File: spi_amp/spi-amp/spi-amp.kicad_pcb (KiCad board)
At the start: 4 copper layers, 26.9 x 69.3 mm, 37 parts, among them J1 IN+, J2 IN-, J3 OUT+, J4 OUT-, J5 Conn_01x02, J7 Conn_01x06, U1 LMH6401, U2 LM78M05_TO220, U3 LTV-847S, U4 74LVC1G04, U5 74LVC1G04, U6 74LVC1G04

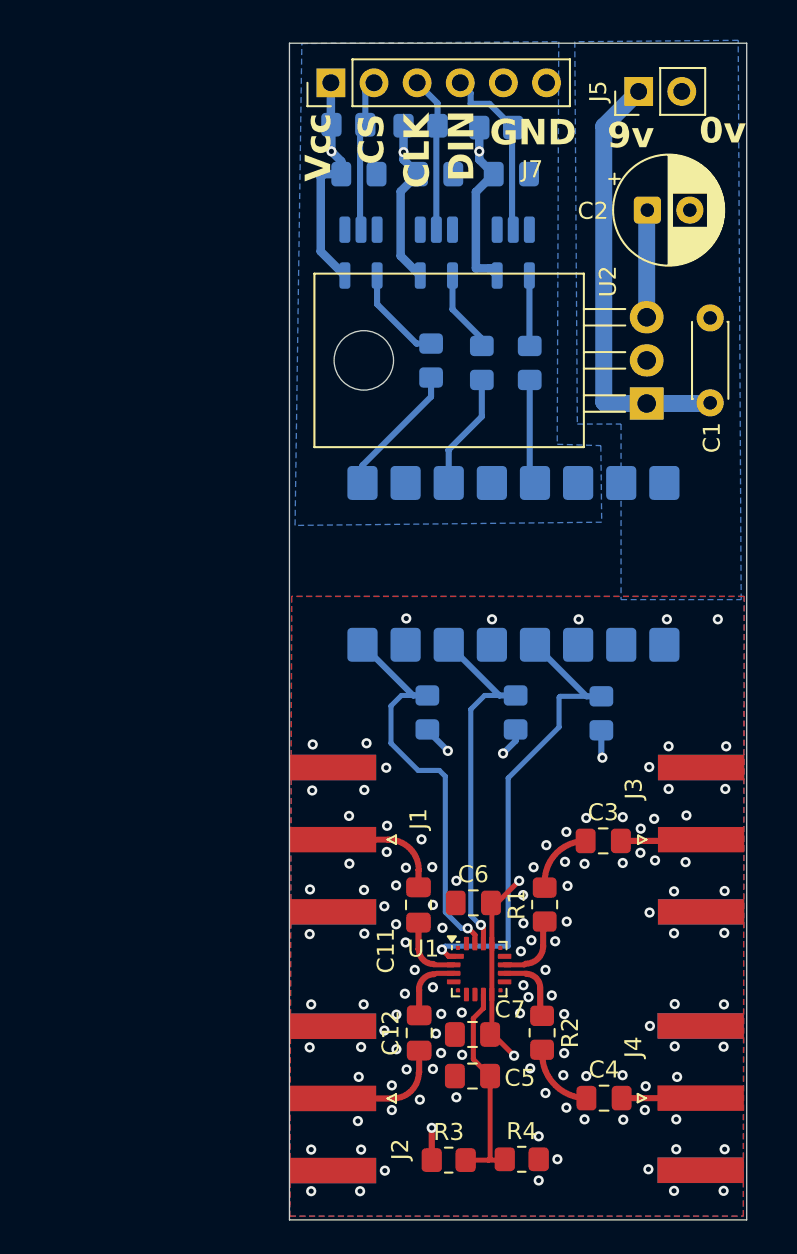
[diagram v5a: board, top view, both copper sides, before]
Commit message: Use 0402 for top layer RF components.
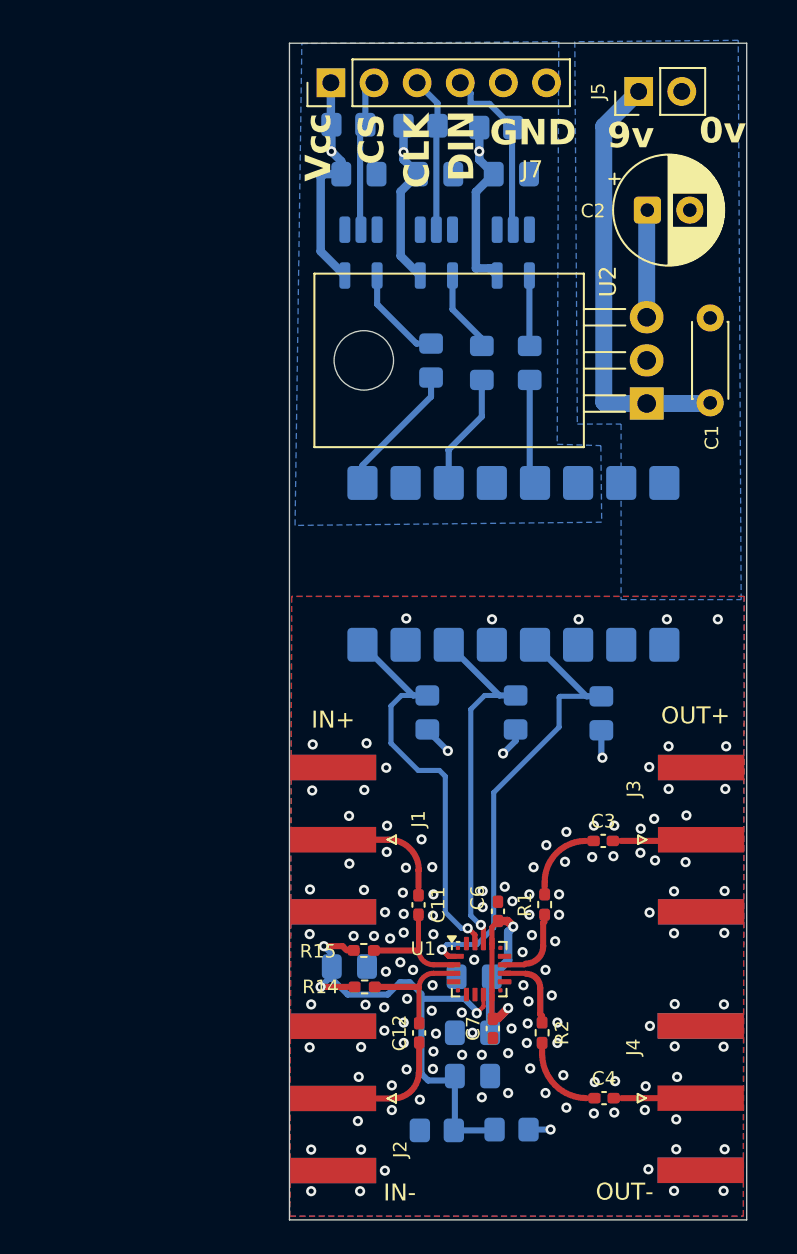
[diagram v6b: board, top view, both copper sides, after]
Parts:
- added C13: 100n, Capacitor_SMD:C_0805_2012Metric_Pad1.18x1.45mm_HandSolder, B.Cu at (109.5, 91.8)
- added C14: 100n, Capacitor_SMD:C_0805_2012Metric_Pad1.18x1.45mm_HandSolder, B.Cu at (116.8, 92.4)
- added C15: 100n, Capacitor_SMD:C_0805_2012Metric_Pad1.18x1.45mm_HandSolder, B.Cu at (116.7, 95.7)
- added R14: 10k, Resistor_SMD:R_0402_1005Metric_Pad0.72x0.64mm_HandSolder, F.Cu at (110.3, 93.0)
- added R15: 10k, Resistor_SMD:R_0402_1005Metric_Pad0.72x0.64mm_HandSolder, F.Cu at (110.3, 90.8)
- C11, C12, C3, C4: footprint Capacitor_SMD:C_0805_2012Metric_Pad1.18x1.45mm_HandSolder -> Capacitor_SMD:C_0402_1005Metric_Pad0.74x0.62mm_HandSolder
- C5, R3, R4: moved to B.Cu
- C6: value 100n -> 2,2n; footprint Capacitor_SMD:C_0805_2012Metric_Pad1.18x1.45mm_HandSolder -> Capacitor_SMD:C_0402_1005Metric_Pad0.74x0.62mm_HandSolder
- C7: value 100n -> 2.2n; footprint Capacitor_SMD:C_0805_2012Metric_Pad1.18x1.45mm_HandSolder -> Capacitor_SMD:C_0402_1005Metric_Pad0.74x0.62mm_HandSolder
- R1, R2: footprint Resistor_SMD:R_0805_2012Metric_Pad1.20x1.40mm_HandSolder -> Resistor_SMD:R_0402_1005Metric_Pad0.72x0.64mm_HandSolder
- moved R4 5.28 mm to (114.6, 101.5), turned to 180 degrees
- moved R3 4.11 mm to (119.0, 101.4), turned to 180 degrees
- moved C6 1.53 mm to (118.2, 88.5), turned to -90 degrees
- moved C7 1.25 mm to (117.9, 95.5), turned to 90 degrees
- turned C5 to 0 degrees
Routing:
- net Net-(U1-Vocm): track 12.8 -> 30.8 mm, vias 0 -> 3
- net VCC: track 25.2 -> 30.0 mm
- net Net-(C12-Pad2): track 3.92 -> 7.22 mm
- net Net-(C11-Pad2): track 4.09 -> 7.33 mm
- net Net-(U1-SDI): track 28.5 -> 27.4 mm
- net DIG_GND: vias 119 -> 132
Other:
- board text added: "IN+"
- board text added: "IN-"
- board text added: "OUT+"
- board text added: "OUT-"

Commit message: Changed to be compatible with EVM.
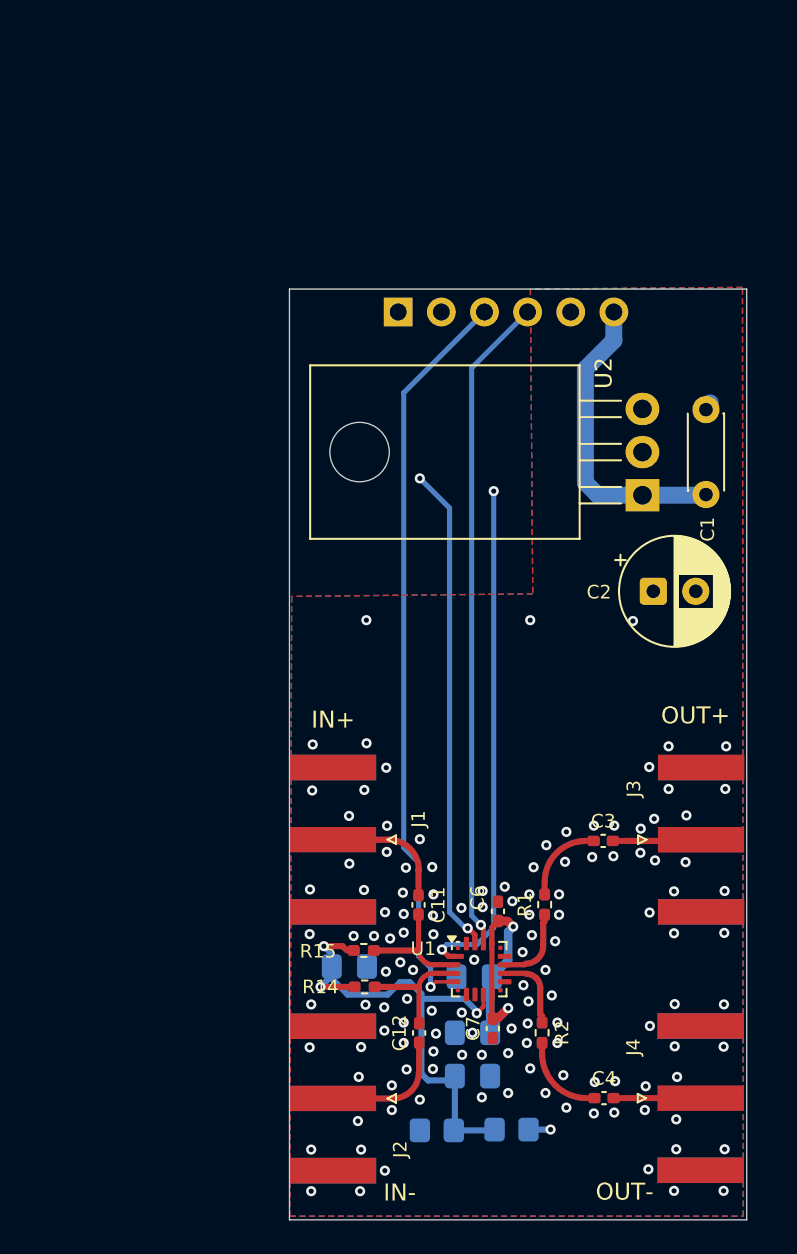
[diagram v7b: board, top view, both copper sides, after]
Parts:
- removed C10, C8, C9: 100n, Capacitor_SMD:C_0805_2012Metric_Pad1.18x1.45mm_HandSolder
- removed J7: Conn_01x06, Connector_PinHeader_2.54mm:PinHeader_1x06_P2.54mm_Vertical
- removed R10, R8, R9: 1.5k, Resistor_SMD:R_0805_2012Metric_Pad1.20x1.40mm_HandSolder
- removed R11, R12, R13: 10k, Resistor_SMD:R_0805_2012Metric_Pad1.20x1.40mm_HandSolder
- removed R5, R6, R7: 1k, Resistor_SMD:R_0805_2012Metric_Pad1.20x1.40mm_HandSolder
- removed U3: LTV-847S, Package_DIP:SMDIP-16_W9.53mm
- removed U4, U5, U6: 74LVC1G04, Package_TO_SOT_SMD:SOT-23-5_HandSoldering
- J5: value Conn_01x02 -> Conn_01x06; footprint Connector_PinHeader_2.54mm:PinHeader_1x02_P2.54mm_Vertical -> Connector_PinSocket_2.54mm:PinSocket_1x06_P2.54mm_Horizontal; moved to B.Cu
- moved C2 22.5 mm to (127.3, 69.7)
- moved J5 19.2 mm to (112.3, 53.2), turned to -90 degrees
- moved U2 5.41 mm to (126.7, 64.0)
- moved C1 5.41 mm to (130.4, 64.0)
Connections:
- C1 pad 1: Net-(J5-Pin_1) -> Net-(J5-Pin_6)
- J5 pad 2: DIG_GND -> Net-(J5-Pin_2)
- U1 pad 1: Net-(U1-SDI) -> Net-(J5-Pin_2)
- U1 pad 14: Net-(U1-CLK) -> Net-(J5-Pin_4)
- U1 pad 15: Net-(U1-CS) -> Net-(J5-Pin_1)
- U1 pad 4: unconnected-(U1-SDO-Pad4) -> Net-(J5-Pin_3)
- U2 pad 1: Net-(J5-Pin_1) -> Net-(J5-Pin_6)
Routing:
- net Net-(J5-Pin_3): track 0.00 -> 43.9 mm, vias 0 -> 1
- net Net-(J5-Pin_2): track 0.00 -> 42.1 mm, vias 0 -> 2
- net Net-(J5-Pin_4): track 0.00 -> 38.9 mm, vias 0 -> 1
- net LED_VCC: track 33.9 -> 0.00 mm, vias 3 -> 0
- net Net-(U1-SDI): track 27.4 -> 0.00 mm, vias 1 -> 0
- net Net-(U1-CS): track 24.5 -> 0.00 mm, vias 1 -> 0
- net Net-(U1-CLK): track 22.3 -> 0.00 mm, vias 1 -> 0
- net Net-(J5-Pin_6): track 0.00 -> 18.2 mm
- net Net-(J5-Pin_1): track 25.5 -> 39.3 mm, vias 0 -> 2
- net VCC: track 30.0 -> 18.6 mm, vias 6 -> 3
- net Net-(J7-Pin_4): track 10.7 -> 0.00 mm
- net Net-(J7-Pin_2): track 9.75 -> 0.00 mm
- net Net-(J7-Pin_3): track 9.18 -> 0.00 mm
- net Net-(R5-Pad1): track 7.88 -> 0.00 mm
- net Net-(R6-Pad1): track 6.89 -> 0.00 mm
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- removed copper zone on In2.Cu, net LED_VCC
- removed copper zone on B.Cu, net SPI_GND
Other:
- board size 26.9 x 69.3 mm -> 26.9 x 54.8 mm
- board text removed: "0v"
- board text removed: "9v"
- board text removed: "CLK"
- board text removed: "CS"
- board text removed: "DIN"
- board text removed: "GND"
- board text removed: "Vcc"

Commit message: ADCIO PCB done.
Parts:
- added H1: MountingHole_Pad, MountingHole:MountingHole_2.7mm_M2.5_Pad, F.Cu at (108.1, 52.9)
- added H2: MountingHole_Pad, MountingHole:MountingHole_2.7mm_M2.5_Pad, F.Cu at (130.5, 52.8)
- moved J3 0.70 mm to (130.9, 84.4)
- moved J4 0.70 mm to (130.8, 99.6)
- moved J5 0.59 mm to (112.7, 52.8)
- moved J1 0.53 mm to (108.0, 84.4)
- moved J2 0.53 mm to (108.0, 99.6)
- moved R14 0.53 mm to (109.8, 93.1)
- moved R15 0.53 mm to (109.8, 90.9)
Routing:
- net Net-(U1-Vocm): track 30.8 -> 31.9 mm
- net Net-(J2-In): track 7.64 -> 8.19 mm
- net Net-(J1-In): track 7.03 -> 7.58 mm
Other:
- board size 26.9 x 54.8 mm -> 28.7 x 64.4 mm
- board text added: "SPI AMP"
